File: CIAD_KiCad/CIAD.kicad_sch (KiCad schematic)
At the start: 23 parts, among them J2 Conn_01x08, SW1 SW_Push, SW10 SW_Push, SW11 SW_Push, SW2 SW_Push, SW3 SW_Push, SW4 SW_Push, SW5 SW_Push, SW6 SW_Push, SW7 SW_Push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

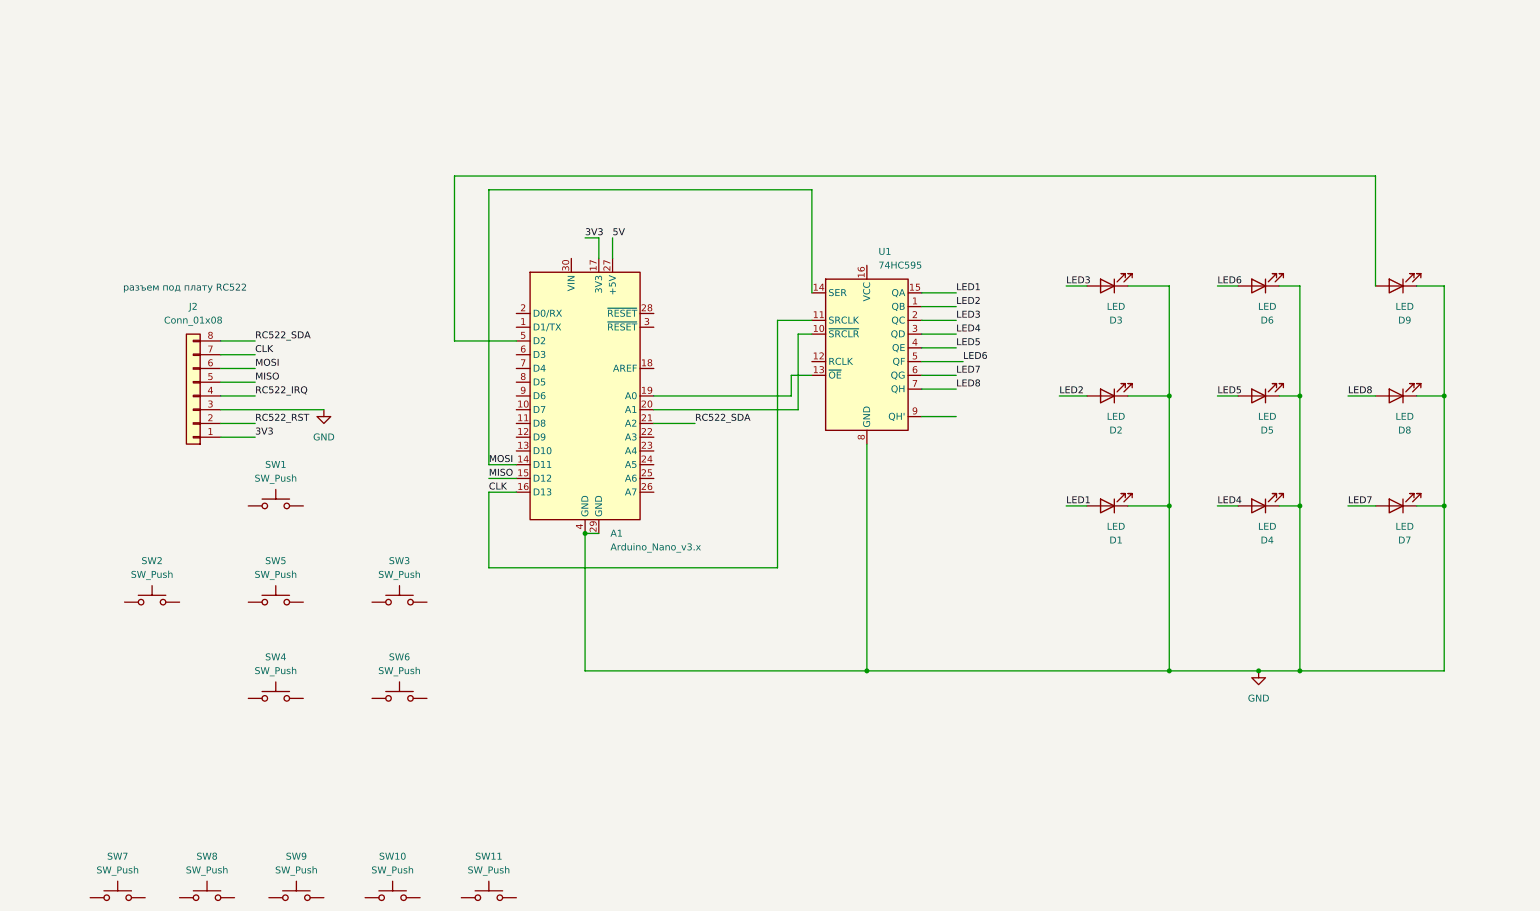
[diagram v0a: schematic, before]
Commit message: Added new libraries for hardware, updated the hardware part
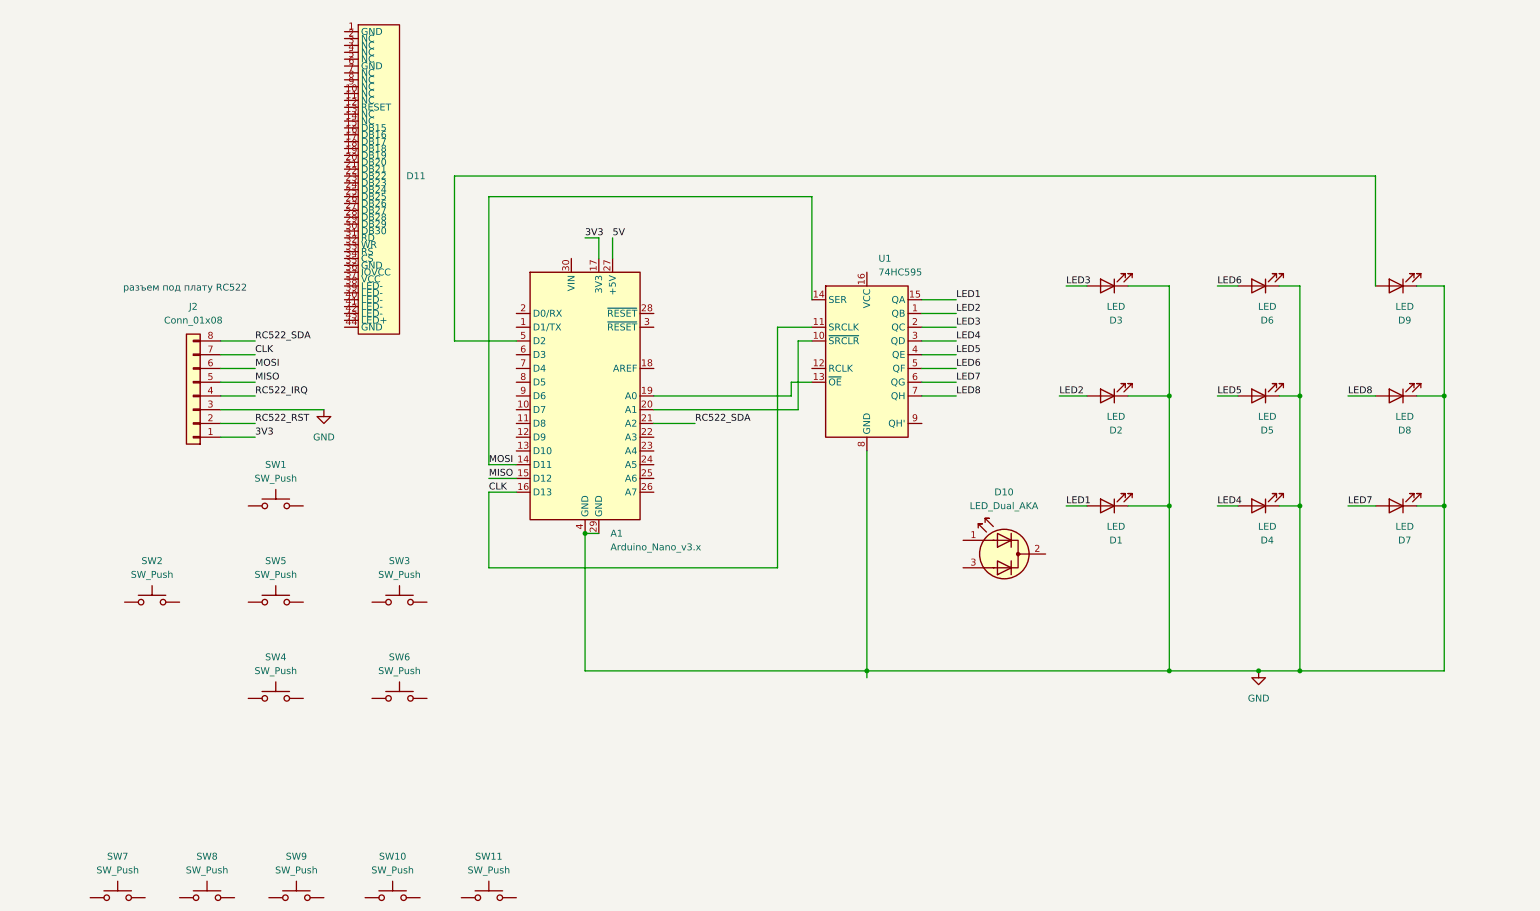
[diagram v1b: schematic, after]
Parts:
- added D10: LED_Dual_AKA, LED_THT:LED_D5.0mm-3, symbol Device:LED_Dual_AKA
- added D11: ~, CIAD:44pin_screen, symbol CIAD:44_pin_screen
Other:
- moved on the sheet: U1

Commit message: updated .gitignore, replaced LEDs in /hardware and fixed connections
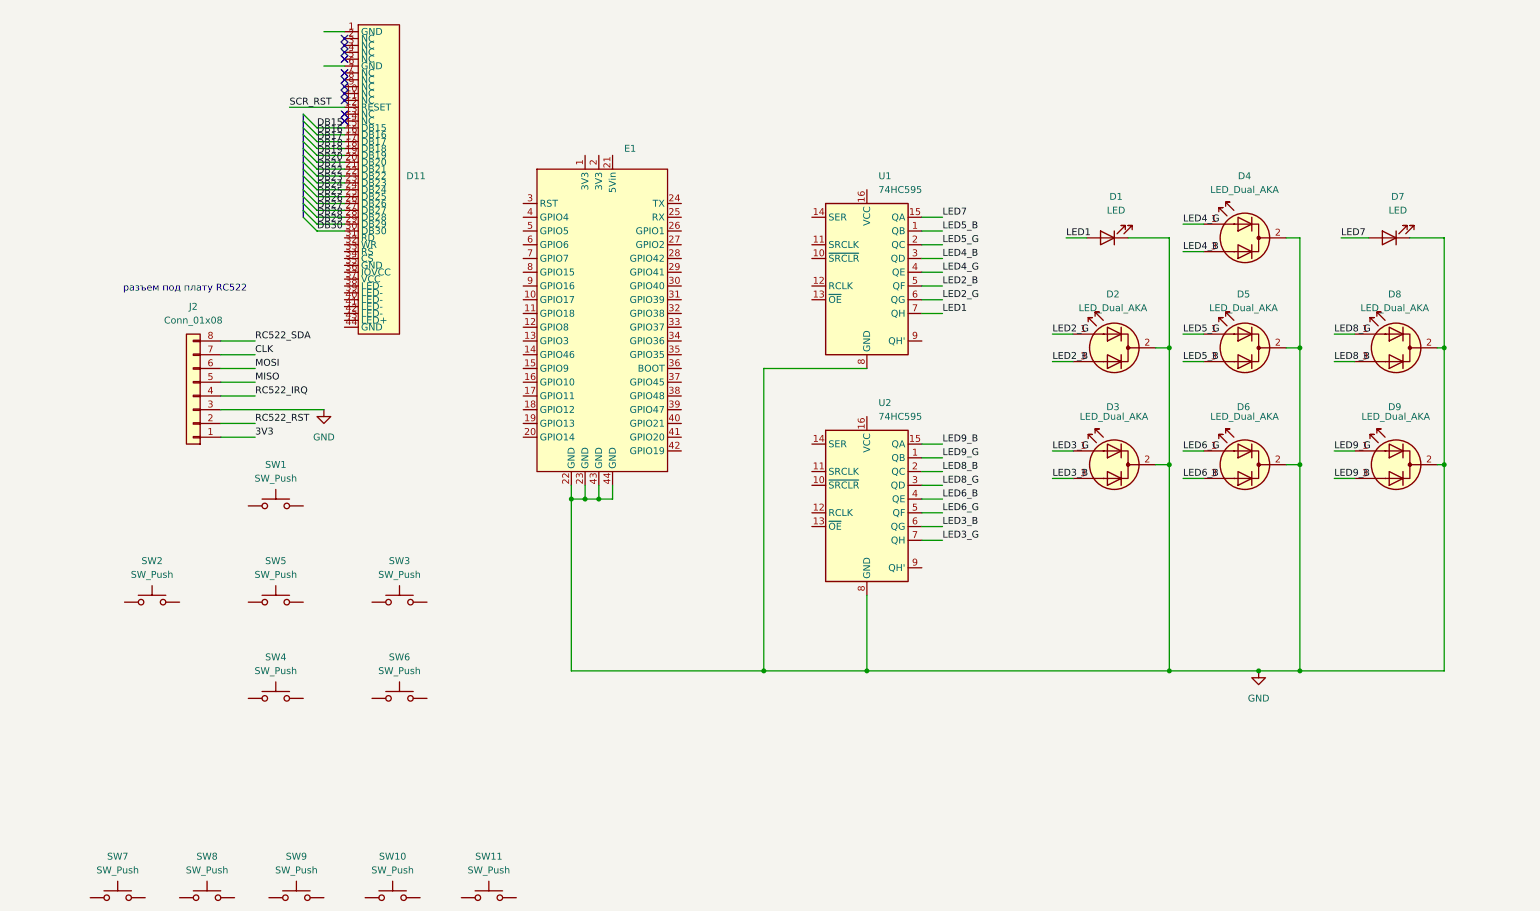
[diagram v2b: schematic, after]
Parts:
- removed A1: Arduino_Nano_v3.x, Module:Arduino_Nano, symbol MCU_Module:Arduino_Nano_v3.x
- removed D10: LED_Dual_AKA, LED_THT:LED_D5.0mm-3, symbol Device:LED_Dual_AKA
- removed D2, D3, D4, D5, D6, D8, D9: LED, LED_THT:LED_D5.0mm, symbol Device:LED
- added D2, D3, D4, D5, D6, D8, D9: LED_Dual_AKA, LED_THT:LED_D5.0mm-3, symbol Device:LED_Dual_AKA
- added E1: ~, symbol CIAD:ESP32
- added U2: 74HC595, Package_DIP:DIP-16_W7.62mm, symbol 74xx:74HC595
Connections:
- net LED8 is gone; now on net LED1: U1.7 (QH)
- net CLK: no longer U1.11 (SRCLK)
- net GND: now also D2.2 (K), D3.2 (K), D4.2 (K), D5.2 (K), D6.2 (K), D8.2 (K), D9.2 (K), E1.22 (GND), E1.23 (GND), E1.43 (GND), E1.44 (GND), U2.8 (GND)
- net LED1: no longer U1.15 (QA)
- net LED7: now also U1.15 (QA); no longer U1.6 (QG)
- net MOSI: no longer U1.14 (SER)
- net SCR_RST: now reaches D11.12 (RESET)
- net DB15: now reaches D11.15 (DB15)
- net DB16: now reaches D11.16 (DB16)
- net DB17: now reaches D11.17 (DB17)
- net DB18: now reaches D11.18 (DB18)
- net DB19: now reaches D11.19 (DB19)
- net DB20: now reaches D11.20 (DB20)
- net DB21: now reaches D11.21 (DB21)
- net DB22: now reaches D11.22 (DB22)
- net DB23: now reaches D11.23 (DB23)
- net DB24: now reaches D11.24 (DB24)
- net DB25: now reaches D11.25 (DB25)
- net DB26: now reaches D11.26 (DB26)
- net DB27: now reaches D11.27 (DB27)
- net DB28: now reaches D11.28 (DB28)
- net DB29: now reaches D11.29 (DB29)
- net DB30: now reaches D11.30 (DB30)
- net LED2 renamed LED5_B
- net LED5_B: now also D5.3 (A2)
- net LED3 renamed LED5_G
- net LED5_G: now also D5.1 (A1)
- net LED4 renamed LED4_B
- net LED4_B: now also D4.3 (A2)
- net LED5 renamed LED4_G
- net LED4_G: now also D4.1 (A1)
- net LED6 renamed LED2_B
- net LED2_B: now also D2.3 (A2)
- new net LED2_G: D2.1 (A1), U1.6 (QG)
- new net LED3_B: D3.3 (A2), U2.6 (QG)
- new net LED3_G: D3.1 (A1), U2.7 (QH)
- new net LED6_B: D6.3 (A2), U2.4 (QE)
- new net LED6_G: D6.1 (A1), U2.5 (QF)
- new net LED8_B: D8.3 (A2), U2.2 (QC)
- new net LED8_G: D8.1 (A1), U2.3 (QD)
- new net LED9_B: D9.3 (A2), U2.15 (QA)
- new net LED9_G: D9.1 (A1), U2.1 (QB)
- no-connect marks 0 -> 11
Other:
- moved on the sheet: U1

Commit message: small updates to hardware
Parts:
- added R1, R2, R3, R4, R5: R, symbol Device:R
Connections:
- net 3V3: now also D11.36 (IOVCC), D11.37 (VCC)
- net GND: now also D11.1 (GND), D11.35 (GND), D11.44 (GND), D11.6 (GND), R1.1, R2.1, R3.1, R4.1, R5.1
- net RD_SCR: now reaches D11.31 (RD)
- net WR_SCR: now reaches D11.32 (WR)
- net RS_SCR: now reaches D11.33 (RS)
- net CS_SCR: now reaches D11.34 (CS)
- net at D11.38 (LED-): now also R1.2
- net at D11.39 (LED-): now also R2.2
- net at D11.40 (LED-): now also R3.2
- net at D11.41 (LED-): now also R4.2
- net at D11.42 (LED-): now also R5.2
- net SCR_RST renamed RST_SCR
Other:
- moved on the sheet: D1, D11, D2, D3, D4, D5, D6, D7, D8, D9, E1, J2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
